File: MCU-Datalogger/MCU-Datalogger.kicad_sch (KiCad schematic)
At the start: 25 parts, among them U1 24LC1025, U2 24LC1025, U3 DS1337S+, U4 ATMEGA328P-AU, Y1 32.768 KHz, Y2 16 MHz

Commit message: add comments to eeschema
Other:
- note added: "EEPROM"
- note added: "MCU"
- note added: "Mounting"
- note added: "Real time clock"
- moved on the sheet: H1, H2, H3, H4
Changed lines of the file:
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@@
+    (stroke (width 0) (type default))
+  )
+  (polyline (pts (xy 140.97 176.53) (xy 29.21 176.53))
     (stroke (width 0) (type default))
   )
@@
     (stroke (width 0) (type default))
   )
+  (polyline (pts (xy 140.97 129.54) (xy 140.97 176.53))
+    (stroke (width 0) (type default))
+  )
   (wire (pts (xy 251.46 44.45) (xy 251.46 48.26))
     (stroke (width 0) (type default))
@@
     (stroke (width 0) (type default))
   )
+  (polyline (pts (xy 29.21 129.54) (xy 29.21 176.53))
+    (stroke (width 0) (type default))
+  )
+  (polyline (pts (xy 124.46 88.9) (xy 124.46 29.21))
+    (stroke (width 0) (type default))
+  )
   (wire (pts (xy 114.3 41.91) (xy 114.3 46.99))
     (stroke (width 0) (type default))
@@
     (stroke (width 0) (type default))
   )
+  (polyline (pts (xy 241.3 156.21) (xy 273.05 156.21))
+    (stroke (width 0) (type default))
+  )
   (wire (pts (xy 215.9 81.28) (xy 220.98 81.28))
     (stroke (width 0) (type default))
@@
     (stroke (width 0) (type default))
   )
+  (polyline (pts (xy 279.4 99.06) (xy 279.4 17.78))
+    (stroke (width 0) (type default))
+  )
   (wire (pts (xy 215.9 83.82) (xy 220.98 83.82))
     (stroke (width 0) (type default))
   )
+  (polyline (pts (xy 128.27 17.78) (xy 279.4 17.78))
+    (stroke (width 0) (type default))
+  )
   (wire (pts (xy 111.76 148.59) (xy 111.76 146.05))
     (stroke (width 0) (type default))
@@
     (stroke (width 0) (type default))
   )
+  (polyline (pts (xy 128.27 17.78) (xy 128.27 99.06))
+    (stroke (width 0) (type default))
+  )
   (wire (pts (xy 251.46 33.02) (xy 265.43 33.02))
     (stroke (width 0) (type default))
   )
+  (polyline (pts (xy 17.78 88.9) (xy 124.46 88.9))
+    (stroke (width 0) (type default))
+  )
   (wire (pts (xy 153.67 29.21) (xy 133.35 29.21))
     (stroke (width 0) (type default))
@@
     (stroke (width 0) (type default))
   )
+  (polyline (pts (xy 17.78 29.21) (xy 17.78 88.9))
+    (stroke (width 0) (type default))
+  )
   (wire (pts (xy 220.98 78.74) (xy 220.98 81.28))
     (stroke (width 0) (type default))
@@
     (stroke (width 0) (type default))
   )
+  (polyline (pts (xy 29.21 129.54) (xy 140.97 129.54))
+    (stroke (width 0) (type default))
+  )
+  (polyline (pts (xy 241.3 111.76) (xy 273.05 111.76))
+    (stroke (width 0) (type default))
+  )
+  (polyline (pts (xy 128.27 99.06) (xy 279.4 99.06))
+    (stroke (width 0) (type default))
+  )
   (wire (pts (xy 222.25 38.1) (xy 222.25 33.02))
     (stroke (width 0) (type default))
@@
     (stroke (width 0) (type default))
   )
+  (polyline (pts (xy 273.05 156.21) (xy 273.05 111.76))
+    (stroke (width 0) (type default))
+  )
   (wire (pts (xy 177.8 63.5) (xy 165.1 63.5))
     (stroke (width 0) (type default))
@@
     (stroke (width 0) (type default))
   )
+  (polyline (pts (xy 241.3 111.76) (xy 241.3 156.21))
+    (stroke (width 0) (type default))
+  )
   (wire (pts (xy 147.32 63.5) (xy 140.97 63.5))
     (stroke (width 0) (type default))
@@
     (stroke (width 0) (type default))
   )
+  (polyline (pts (xy 124.46 29.21) (xy 17.78 29.21))
+    (stroke (width 0) (type default))
+  )
   (wire (pts (xy 71.12 161.29) (xy 86.36 161.29))
     (stroke (width 0) (type default))
   )
+  (text "EEPROM" (at 29.21 128.27 0)
+    (effects (font (size 1.27 1.27)) (justify left bottom))
+  )
+  (text "Mounting" (at 241.3 110.49 0)
+    (effects (font (size 1.27 1.27)) (justify left bottom))
+  )
+  (text "MCU" (at 127.635 16.51 0)
+    (effects (font (size 1.27 1.27)) (justify left bottom))
+  )
+  (text "Real time clock" (at 17.78 28.575 0)
+    (effects (font (size 1.27 1.27)) (justify left bottom))
+  )
   (label "Vcc" (at 41.91 149.86 180) (fields_autoplaced)
     (effects (font (size 1.27 1.27)) (justify right bottom))
@@
     )
   )
-  (symbol (lib_id "Mechanical:MountingHole") (at 257.81 123.19 0) (unit 1)
-    (in_bom yes) (on_board yes) (dnp no) (fields_autoplaced)
-    (property "Reference" "H1" (at 260.35 121.92 0)
-      (effects (font (size 1.27 1.27)) (justify left))
-    )
-    (property "Value" "MountingHole" (at 260.35 124.46 0)
-      (effects (font (size 1.27 1.27)) (justify left))
-    )
-    (property "Footprint" "MountingHole:MountingHole_2.1mm" (at 257.81 123.19 0)
-      (effects (font (size 1.27 1.27)) hide)
-    )
-    (property "Datasheet" "~" (at 257.81 123.19 0)
+  (symbol (lib_id "Mechanical:MountingHole") (at 248.92 116.84 0) (unit 1)
+    (in_bom yes) (on_board yes) (dnp no) (fields_autoplaced)
+    (property "Reference" "H1" (at 251.46 115.57 0)
+      (effects (font (size 1.27 1.27)) (justify left))
+    )
+    (property "Value" "MountingHole" (at 251.46 118.11 0)
+      (effects (font (size 1.27 1.27)) (justify left))
+    )
+    (property "Footprint" "MountingHole:MountingHole_2.1mm" (at 248.92 116.84 0)
+      (effects (font (size 1.27 1.27)) hide)
+    )
+    (property "Datasheet" "~" (at 248.92 116.84 0)
       (effects (font (size 1.27 1.27)) hide)
     )
@@
     )
   )
-  (symbol (lib_id "Mechanical:MountingHole") (at 257.81 133.35 0) (unit 1)
-    (in_bom yes) (on_board yes) (dnp no) (fields_autoplaced)
-    (property "Reference" "H2" (at 260.35 132.08 0)
-      (effects (font (size 1.27 1.27)) (justify left))
-    )
-    (property "Value" "MountingHole" (at 260.35 134.62 0)
-      (effects (font (size 1.27 1.27)) (justify left))
-    )
-    (property "Footprint" "MountingHole:MountingHole_2.1mm" (at 257.81 133.35 0)
-      (effects (font (size 1.27 1.27)) hide)
-    )
-    (property "Datasheet" "~" (at 257.81 133.35 0)
+  (symbol (lib_id "Mechanical:MountingHole") (at 248.92 127 0) (unit 1)
+    (in_bom yes) (on_board yes) (dnp no) (fields_autoplaced)
+    (property "Reference" "H2" (at 251.46 125.73 0)
+      (effects (font (size 1.27 1.27)) (justify left))
+    )
+    (property "Value" "MountingHole" (at 251.46 128.27 0)
+      (effects (font (size 1.27 1.27)) (justify left))
+    )
+    (property "Footprint" "MountingHole:MountingHole_2.1mm" (at 248.92 127 0)
+      (effects (font (size 1.27 1.27)) hide)
+    )
+    (property "Datasheet" "~" (at 248.92 127 0)
       (effects (font (size 1.27 1.27)) hide)
     )
@@
     )
   )
-  (symbol (lib_id "Mechanical:MountingHole") (at 257.81 144.78 0) (unit 1)
-    (in_bom yes) (on_board yes) (dnp no) (fields_autoplaced)
-    (property "Reference" "H3" (at 260.35 143.51 0)
-      (effects (font (size 1.27 1.27)) (justify left))
-    )
-    (property "Value" "MountingHole" (at 260.35 146.05 0)
-      (effects (font (size 1.27 1.27)) (justify left))
-    )
-    (property "Footprint" "MountingHole:MountingHole_2.1mm" (at 257.81 144.78 0)
-      (effects (font (size 1.27 1.27)) hide)
-    )
-    (property "Datasheet" "~" (at 257.81 144.78 0)
+  (symbol (lib_id "Mechanical:MountingHole") (at 248.92 138.43 0) (unit 1)
+    (in_bom yes) (on_board yes) (dnp no) (fields_autoplaced)
+    (property "Reference" "H3" (at 251.46 137.16 0)
+      (effects (font (size 1.27 1.27)) (justify left))
+    )
+    (property "Value" "MountingHole" (at 251.46 139.7 0)
+      (effects (font (size 1.27 1.27)) (justify left))
+    )
+    (property "Footprint" "MountingHole:MountingHole_2.1mm" (at 248.92 138.43 0)
+      (effects (font (size 1.27 1.27)) hide)
+    )
+    (property "Datasheet" "~" (at 248.92 138.43 0)
       (effects (font (size 1.27 1.27)) hide)
     )
@@
     )
   )
-  (symbol (lib_id "Mechanical:MountingHole") (at 257.81 156.21 0) (unit 1)
-    (in_bom yes) (on_board yes) (dnp no) (fields_autoplaced)
-    (property "Reference" "H4" (at 260.35 154.94 0)
-      (effects (font (size 1.27 1.27)) (justify left))
-    )
-    (property "Value" "MountingHole" (at 260.35 157.48 0)
-      (effects (font (size 1.27 1.27)) (justify left))
-    )
-    (property "Footprint" "MountingHole:MountingHole_2.1mm" (at 257.81 156.21 0)
-      (effects (font (size 1.27 1.27)) hide)
-    )
-    (property "Datasheet" "~" (at 257.81 156.21 0)
-      (effects (font (size 1.27 1.27)) hide)
-    )
+  (symbol (lib_id "Mechanical:MountingHole") (at 248.92 149.86 0) (unit 1)
+    (in_bom yes) (on_board yes) (dnp no) (fields_autoplaced)
+    (property "Reference" "H4" (at 251.46 148.59 0)
+      (effects (font (size 1.27 1.27)) (justify left))
+    )
+    (property "Value" "MountingHole" (at 251.46 151.13 0)
+      (effects (font (size 1.27 1.27)) (justify left))
+    )
+    (property "Footprint" "MountingHole:MountingHole_2.1mm" (at 248.92 149.86 0)
+      (effects (font (size 1.27 1.27)) hide)
+    )
+    (property "Datasheet" "~" (at 248.92 149.86 0)
+      (effects (font (size 1.27 1.27)) hide)
+    )

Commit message: Roututing
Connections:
- net SCK: now also D2.2 (A), U4.17 (PB5)
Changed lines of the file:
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@@
+    (effects (font (size 1.27 1.27)) (justify right bottom))
+  )
+  (label "SCK" (at 184.785 53.34 180) (fields_autoplaced)
     (effects (font (size 1.27 1.27)) (justify right bottom))
   )

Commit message: fixed outstanding issues
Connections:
- net Vcc: now also BT1.1 (+), C5.1, D1.2 (A), U4.18 (AVCC), U4.4 (VCC)
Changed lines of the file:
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@@
+    (effects (font (size 1.27 1.27)) (justify left bottom))
+  )
+  (label "Vcc" (at 243.84 33.02 0) (fields_autoplaced)
     (effects (font (size 1.27 1.27)) (justify left bottom))
   )

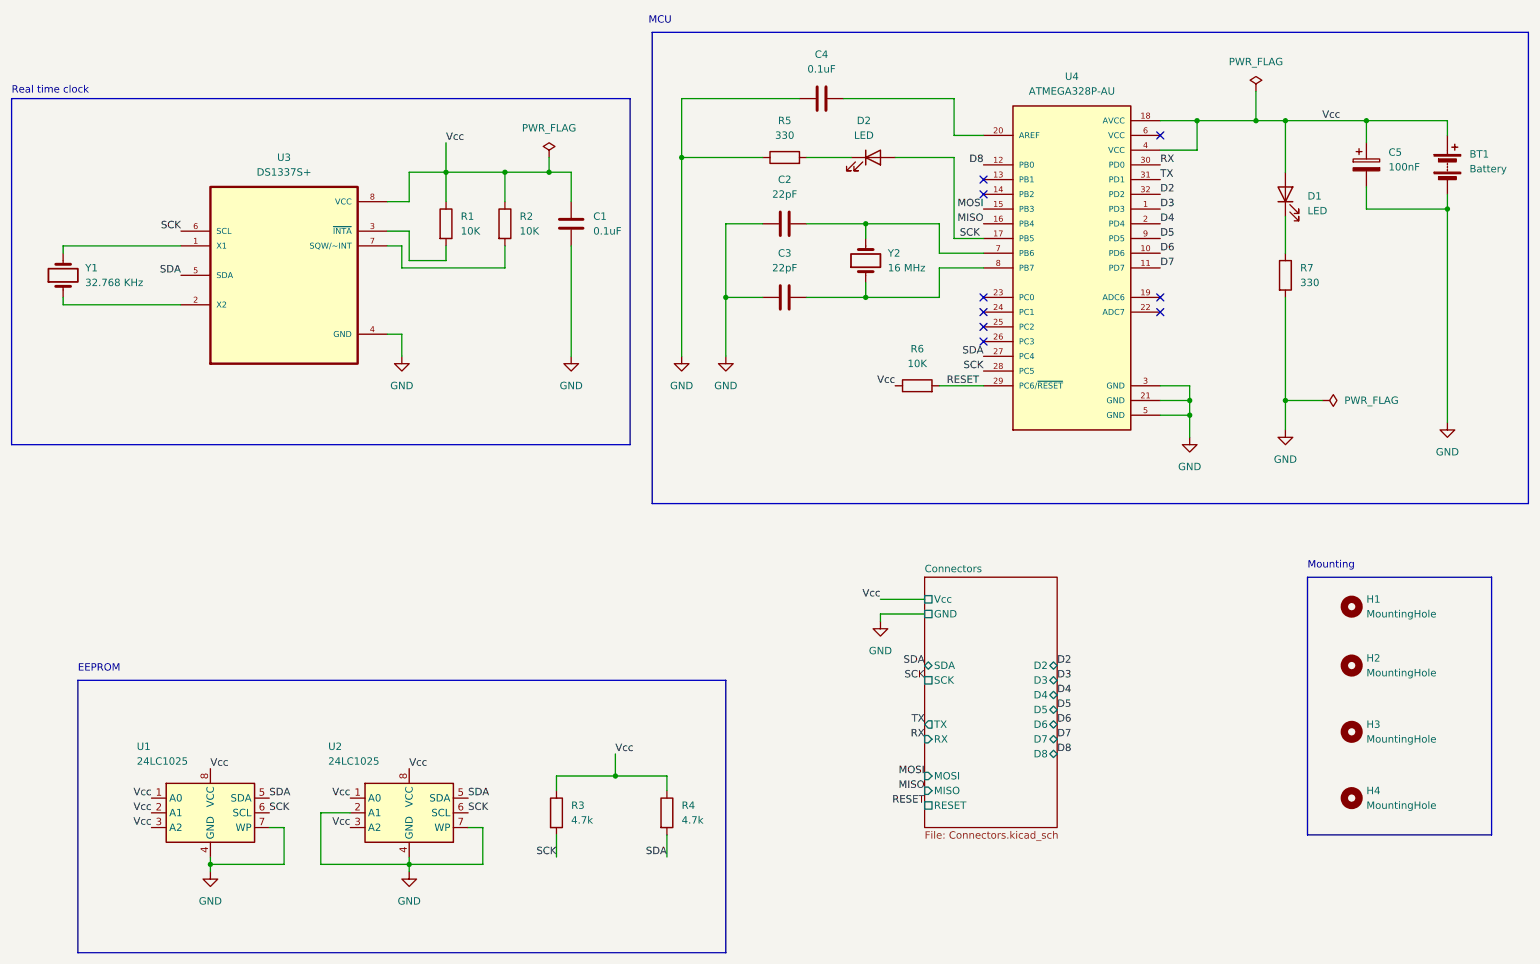
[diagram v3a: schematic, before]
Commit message: modified SCL to SCK Label because of wrong pin was choosen
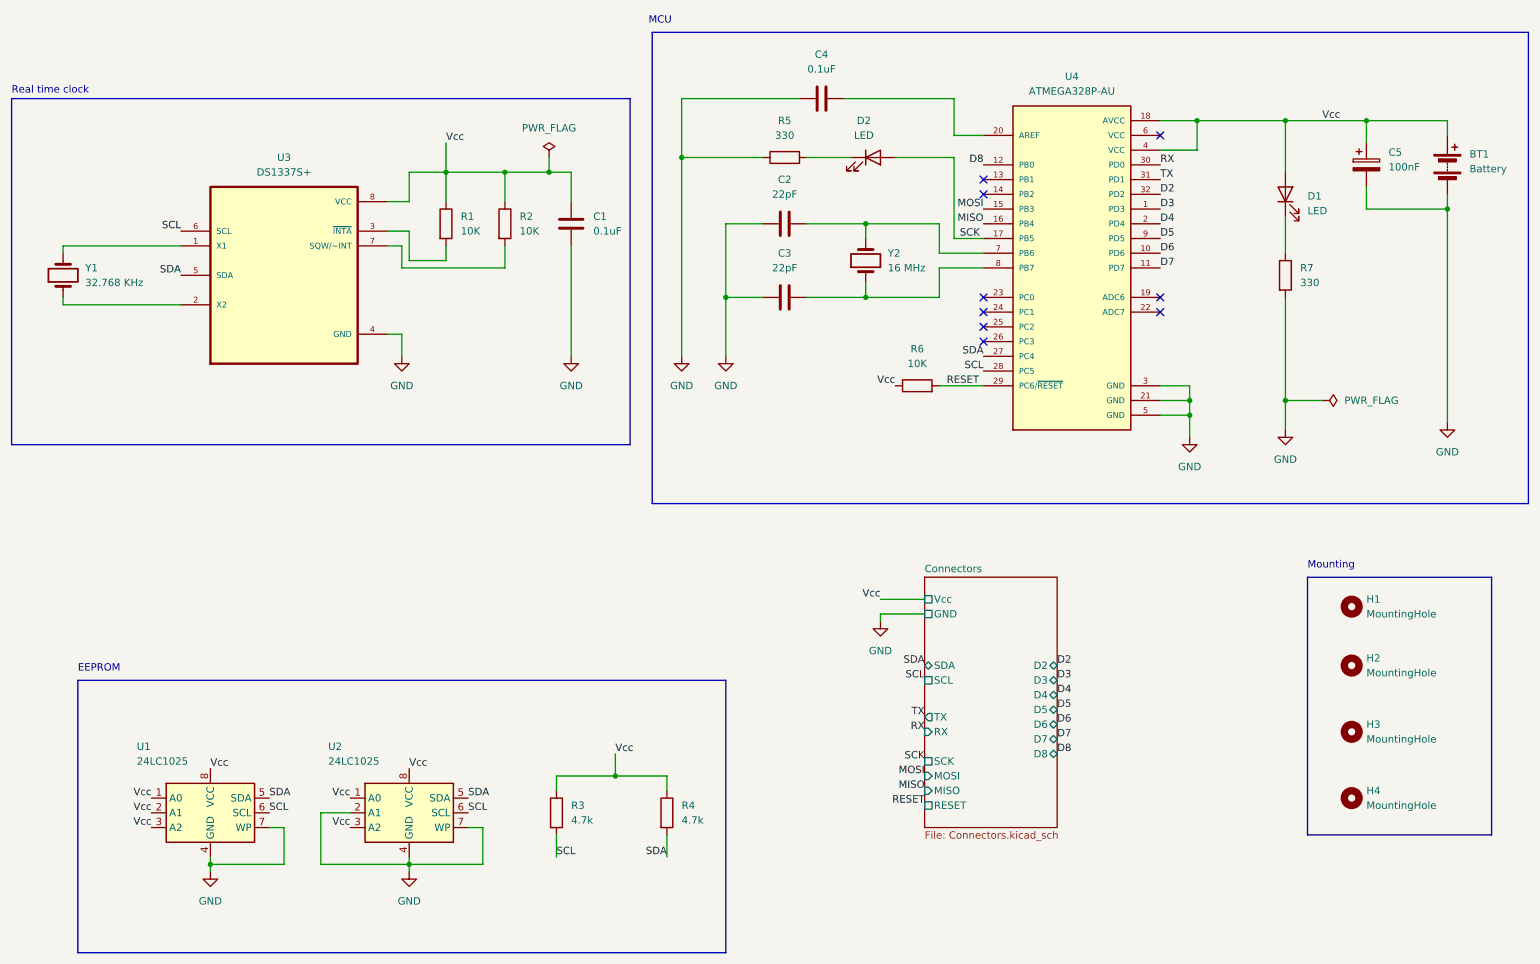
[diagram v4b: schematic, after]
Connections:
- net SCK: no longer R3.2, U1.6 (SCL), U2.6 (SCL), U3.6 (SCL), U4.28 (PC5)
- new net SCL: R3.2, U1.6 (SCL), U2.6 (SCL), U3.6 (SCL), U4.28 (PC5)
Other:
- sheet Connectors ports: added SCL; removed none
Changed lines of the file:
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@@
   (junction (at 86.36 161.29) (diameter 0) (color 0 0 0 0)
-  )
-  (junction (at 232.41 33.02) (diameter 0) (color 0 0 0 0)
   )
   (junction (at 110.49 41.91) (diameter 0) (color 0 0 0 0)
@@
     (stroke (width 0) (type default))
   )
-  (wire (pts (xy 222.25 33.02) (xy 232.41 33.02))
-    (stroke (width 0) (type default))
-  )
-  (wire (pts (xy 232.41 27.94) (xy 232.41 33.02))
+  (wire (pts (xy 222.25 33.02) (xy 237.49 33.02))
     (stroke (width 0) (type default))
   )
@@
     (stroke (width 0) (type default))
   )
-  (wire (pts (xy 232.41 33.02) (xy 237.49 33.02))
-    (stroke (width 0) (type default))
-  )
   (wire (pts (xy 82.55 52.07) (xy 86.36 52.07))
     (stroke (width 0) (type default))
@@
     (effects (font (size 1.27 1.27)) (justify left bottom))
   )
-  (label "SCK" (at 46.99 52.07 180) (fields_autoplaced)
-    (effects (font (size 1.27 1.27)) (justify right bottom))
-  )
   (label "MISO" (at 175.26 148.59 180) (fields_autoplaced)
     (effects (font (size 1.27 1.27)) (justify right bottom))
@@
     (effects (font (size 1.27 1.27)) (justify left bottom))
   )
-  (label "SCK" (at 111.76 160.02 180) (fields_autoplaced)
-    (effects (font (size 1.27 1.27)) (justify right bottom))
-  )
   (label "SCK" (at 184.785 53.34 180) (fields_autoplaced)
     (effects (font (size 1.27 1.27)) (justify right bottom))
@@
     (effects (font (size 1.27 1.27)) (justify left bottom))
   )
+  (label "SCK" (at 175.26 143.51 180) (fields_autoplaced)
+    (effects (font (size 1.27 1.27)) (justify right bottom))
+  )
   (label "D4" (at 215.9 50.8 0) (fields_autoplaced)
     (effects (font (size 1.27 1.27)) (justify left bottom))
@@
     (effects (font (size 1.27 1.27)) (justify right bottom))
   )
-  (label "RX" (at 175.26 139.7 180) (fields_autoplaced)
-    (effects (font (size 1.27 1.27)) (justify right bottom))
+  (label "RX" (at 175.26 138.43 180) (fields_autoplaced)
+    (effects (font (size 1.27 1.27)) (justify right bottom))
+  )
+  (label "SCL" (at 62.23 152.4 0) (fields_autoplaced)
+    (effects (font (size 1.27 1.27)) (justify left bottom))
   )
   (label "Vcc" (at 41.91 154.94 180) (fields_autoplaced)
     (effects (font (size 1.27 1.27)) (justify right bottom))
   )
-  (label "SCK" (at 62.23 152.4 0) (fields_autoplaced)
-    (effects (font (size 1.27 1.27)) (justify left bottom))
-  )
   (label "RESET" (at 175.26 151.13 180) (fields_autoplaced)
     (effects (font (size 1.27 1.27)) (justify right bottom))
@@
     (effects (font (size 1.27 1.27)) (justify right bottom))
   )
-  (label "SCK" (at 96.52 152.4 0) (fields_autoplaced)
-    (effects (font (size 1.27 1.27)) (justify left bottom))
+  (label "SCL" (at 175.26 129.54 180) (fields_autoplaced)
+    (effects (font (size 1.27 1.27)) (justify right bottom))
   )
   (label "Vcc" (at 76.2 149.86 180) (fields_autoplaced)
@@
     (effects (font (size 1.27 1.27)) (justify left bottom))
   )
-  (label "TX" (at 175.26 137.16 180) (fields_autoplaced)
-    (effects (font (size 1.27 1.27)) (justify right bottom))
-  )
-  (label "SCK" (at 175.26 129.54 180) (fields_autoplaced)
+  (label "TX" (at 175.26 135.89 180) (fields_autoplaced)
     (effects (font (size 1.27 1.27)) (justify right bottom))
   )
@@
     (effects (font (size 1.27 1.27)) (justify left bottom))
   )
+  (label "SCL" (at 46.99 52.07 180) (fields_autoplaced)
+    (effects (font (size 1.27 1.27)) (justify right bottom))
+  )
+  (label "SCL" (at 96.52 152.4 0) (fields_autoplaced)
+    (effects (font (size 1.27 1.27)) (justify left bottom))
+  )
   (label "RESET" (at 179.07 78.74 0) (fields_autoplaced)
     (effects (font (size 1.27 1.27)) (justify left bottom))
@@
     (effects (font (size 1.27 1.27)) (justify left bottom))
   )
-  (label "SCK" (at 185.42 76.2 180) (fields_autoplaced)
+  (label "SCL" (at 185.42 76.2 180) (fields_autoplaced)
     (effects (font (size 1.27 1.27)) (justify right bottom))
   )
@@
   )
   (label "RX" (at 215.9 40.64 0) (fields_autoplaced)
+    (effects (font (size 1.27 1.27)) (justify left bottom))
+  )
+  (label "SCL" (at 111.76 160.02 0) (fields_autoplaced)
     (effects (font (size 1.27 1.27)) (justify left bottom))
   )
@@
     )
   )
-  (symbol (lib_id "power:PWR_FLAG") (at 232.41 27.94 0) (unit 1)
-    (in_bom yes) (on_board yes) (dnp no) (fields_autoplaced)
-    (property "Reference" "#FLG01" (at 232.41 26.035 0)
-      (effects (font (size 1.27 1.27)) hide)
-    )
-    (property "Value" "PWR_FLAG" (at 232.41 22.86 0)
-      (effects (font (size 1.27 1.27)))
-    )
-    (property "Footprint" "" (at 232.41 27.94 0)
-      (effects (font (size 1.27 1.27)) hide)
-    )
-    (property "Datasheet" "~" (at 232.41 27.94 0)
-      (effects (font (size 1.27 1.27)) hide)
-    )
-    (pin "1")
-    (instances
-      (project "MCU-Datalogger"
-        (path "/ff08e7c5-b4dc-4c9c-b680-b2226ed71bf7"
-          (reference "#FLG01") (unit 1)
-        )
-      )
-    )
-  )
   (symbol (lib_id "power:GND") (at 167.64 119.38 0) (unit 1)
     (in_bom yes) (on_board yes) (dnp no) (fields_autoplaced)
@@
       (effects (font (size 1.27 1.27)) (justify left))
     )
-    (pin "SCK" passive (at 175.26 129.54 180)
-      (effects (font (size 1.27 1.27)) (justify left))
-    )
     (pin "GND" passive (at 175.26 118.11 180)
       (effects (font (size 1.27 1.27)) (justify left))
@@
       (effects (font (size 1.27 1.27)) (justify right))
     )
-    (pin "TX" output (at 175.26 137.16 180)
-      (effects (font (size 1.27 1.27)) (justify left))
-    )
-    (pin "RX" input (at 175.26 139.7 180)
+    (pin "TX" output (at 175.26 135.89 180)
+      (effects (font (size 1.27 1.27)) (justify left))
+    )
+    (pin "RX" input (at 175.26 138.43 180)
       (effects (font (size 1.27 1.27)) (justify left))
     )
@@
       (effects (font (size 1.27 1.27)) (justify left))
     )
+    (pin "SCK" passive (at 175.26 143.51 180)
+      (effects (font (size 1.27 1.27)) (justify left))
+    )
+    (pin "SCL" passive (at 175.26 129.54 180)
+      (effects (font (size 1.27 1.27)) (justify left))
+    )
